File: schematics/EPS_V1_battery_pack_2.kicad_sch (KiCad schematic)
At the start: 31 parts, among them U8 MP2672AGD-0000-Z, U9 MAX17205G+

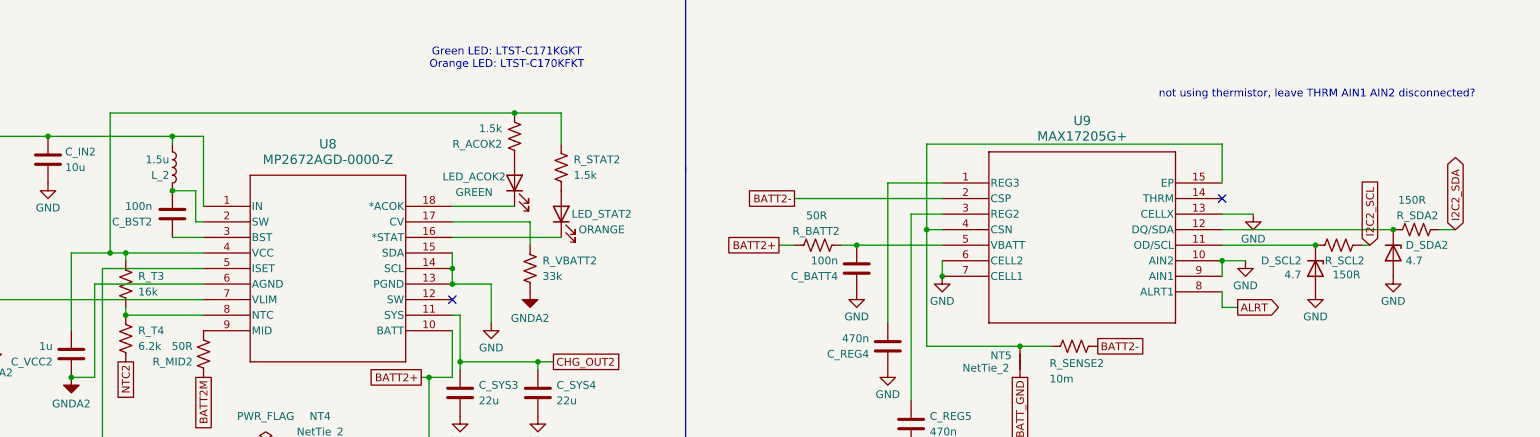
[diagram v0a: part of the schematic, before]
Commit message: Switch out MP28167 for LTC3119 (MPPC buck-boost) in schematic
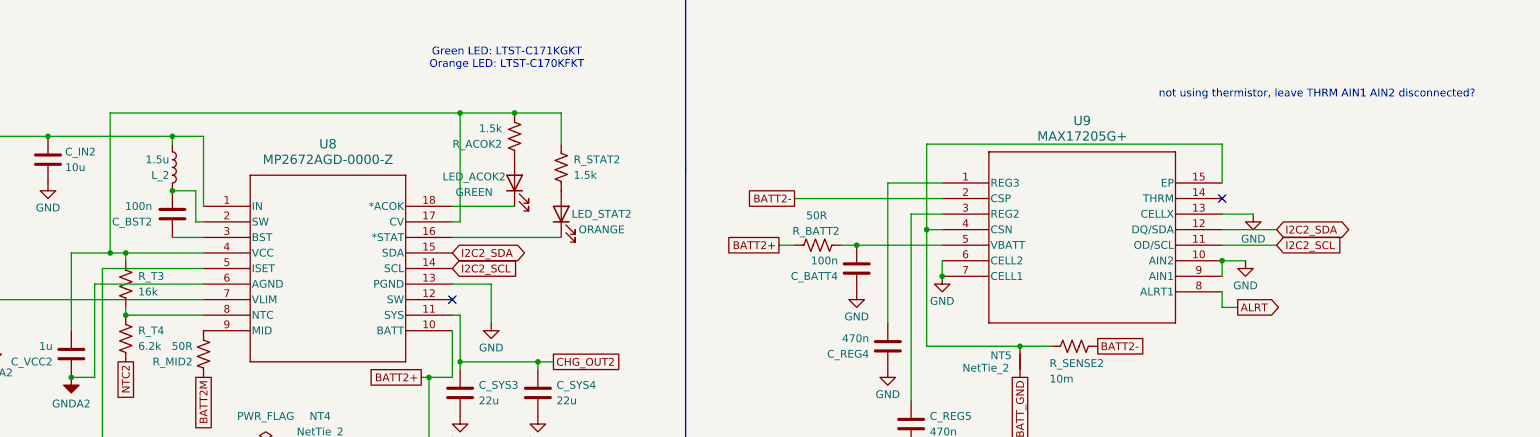
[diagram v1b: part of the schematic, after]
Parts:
- removed D_SCL2, D_SDA2: 4.7, Diode_SMD:D_0603_1608Metric, symbol Device:D_Zener
- removed R_SCL2, R_SDA2: 150R, Resistor_SMD:R_0603_1608Metric, symbol Device:R_US
- removed R_VBATT2: 33k, Resistor_SMD:R_0603_1608Metric, symbol Device:R_US
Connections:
- net GND: no longer U8.14 (SCL), U8.15 (SDA)
- net I2C2_SCL: now also U8.14 (SCL), U9.11 (OD/SCL)
- net I2C2_SDA: now also U8.15 (SDA), U9.12 (DQ/SDA)
- net at C_VCC2.2, R_ACOK2.2, R_STAT2.1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: now also U8.17 (CV)
